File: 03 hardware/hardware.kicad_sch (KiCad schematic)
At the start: 7 parts, among them SW3 SW_MEC_5G, U1 PIC16F877A-IP, Y1 16Mhz

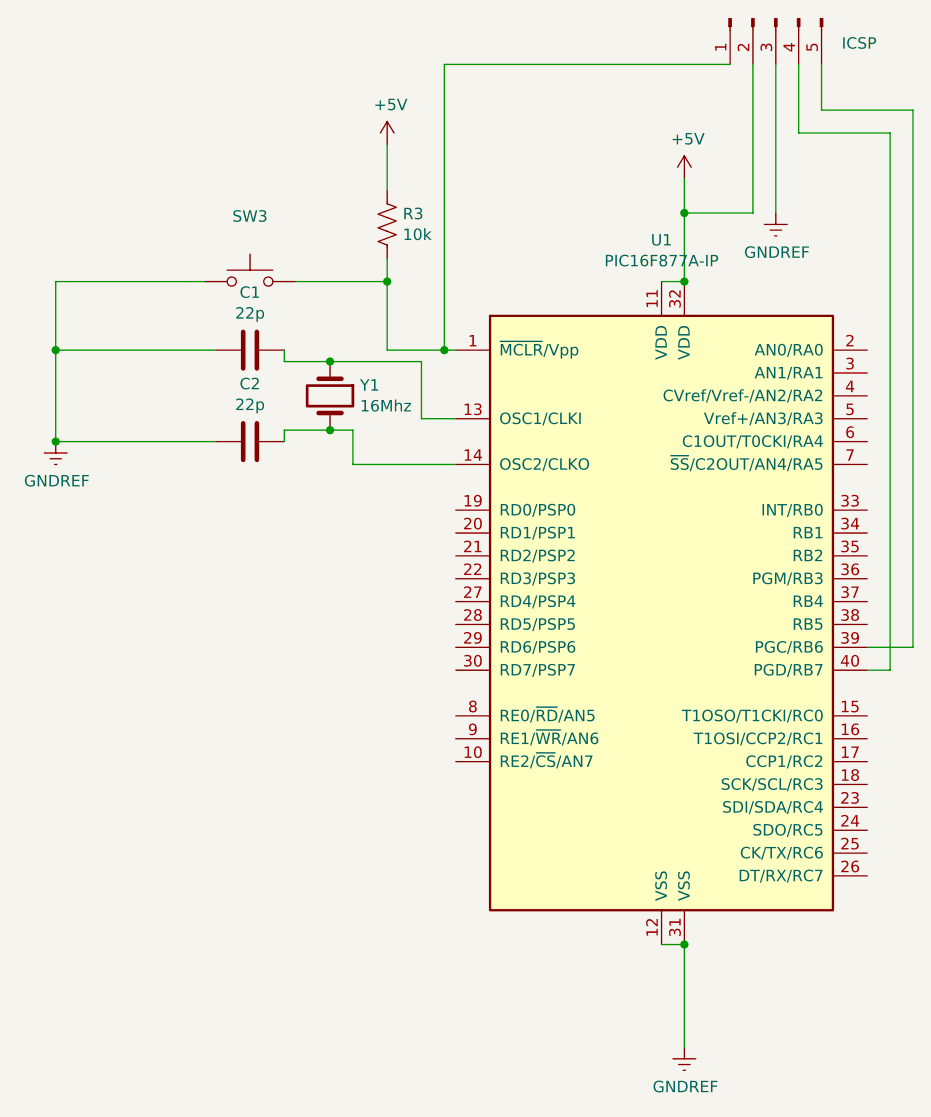
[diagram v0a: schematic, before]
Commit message: 05 Blinky and Running LEDs
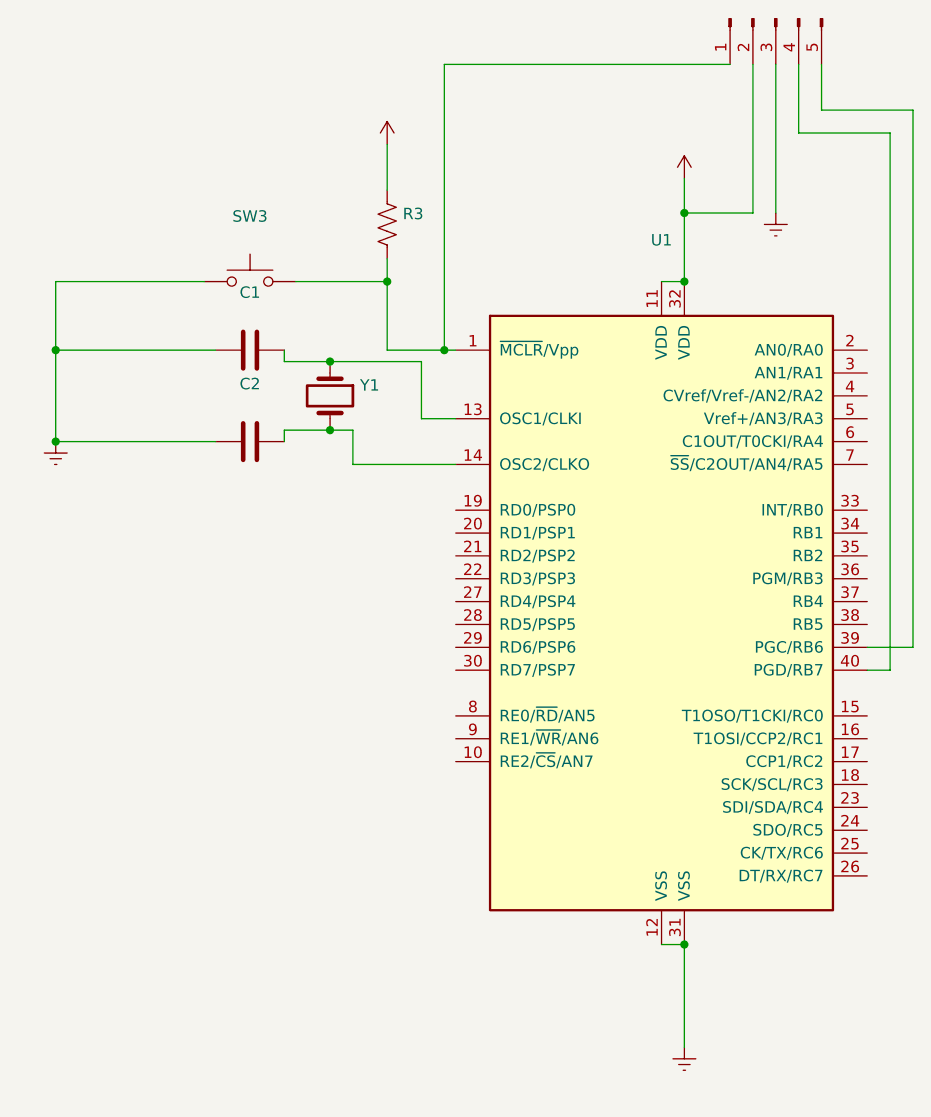
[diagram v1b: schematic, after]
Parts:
- C1, C2: value 22p -> (none)
- ICSP1: value ICSP -> (none)
- R3: value 10k -> (none)
- SW3: value SW_MEC_5G -> (none)
- U1: value PIC16F877A-IP -> (none)
- Y1: value 16Mhz -> (none)
